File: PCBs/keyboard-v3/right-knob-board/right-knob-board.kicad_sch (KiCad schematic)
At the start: 36 parts, among them J101 F31L-1A7H1-11008, M1 2206-100T, Q101 DMP21D0UFB-7B, Q102 DMP21D0UFB-7B, Q201 DMN21D2UFB-7B, SW1 SW_DIP_x01, SW2 SW_DIP_x01, SW3 SW_DIP_x01, U101 TMC6300-LA, U102 AS5600, U103 STM32U031C6Ux

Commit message: Right control board placement and schematic done
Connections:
- net DIAG: now also U103.25 (PB12); no longer U103.21 (PB10)
- net STANDBY: now also U103.21 (PB10); no longer U103.25 (PB12)
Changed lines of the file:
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@@
 	(wire
 		(pts
-			(xy 35.56 172.72) (xy 48.26 172.72)
-		)
-		(stroke
-			(width 0)
-			(type default)
-		)
-	)
-	(wire
-		(pts
 			(xy 88.9 55.88) (xy 76.2 55.88)
 		)
@@
 	(wire
 		(pts
-			(xy 35.56 177.8) (xy 48.26 177.8)
-		)
-		(stroke
-			(width 0)
-			(type default)
-		)
-	)
-	(wire
-		(pts
 			(xy 139.7 106.68) (xy 139.7 116.84)
 		)
@@
 	(wire
 		(pts
+			(xy 35.56 172.72) (xy 48.26 172.72)
+		)
+		(stroke
+			(width 0)
+			(type default)
+		)
+	)
+	(wire
+		(pts
 			(xy 114.3 96.52) (xy 114.3 99.06)
 		)
@@
 	(wire
 		(pts
+			(xy 35.56 177.8) (xy 48.26 177.8)
+		)
+		(stroke
+			(width 0)
+			(type default)
+		)
+	)
+	(wire
+		(pts
 			(xy 93.98 165.1) (xy 96.52 165.1)
 		)
@@
 		)
 	)
+	(label "DIAG"
+		(at 35.56 177.8 0)
+		(effects
+			(font
+				(size 1.27 1.27)
+			)
+			(justify left bottom)
+		)
+	)
 	(label "STANDBY"
 		(at 167.64 147.32 0)
@@
 		)
 	)
+	(label "STANDBY"
+		(at 35.56 172.72 0)
+		(effects
+			(font
+				(size 1.27 1.27)
+			)
+			(justify left bottom)
+		)
+	)
 	(label "LED2"
 		(at 203.2 45.72 0)
@@
 		)
 	)
-	(label "STANDBY"
-		(at 35.56 177.8 0)
-		(effects
-			(font
-				(size 1.27 1.27)
-			)
-			(justify left bottom)
-		)
-	)
 	(label "DIAG"
 		(at 190.5 134.62 0)
@@
 		)
 	)
-	(label "DIAG"
-		(at 35.56 172.72 0)
-		(effects
-			(font
-				(size 1.27 1.27)
-			)
-			(justify left bottom)
-		)
-	)
 	(label "TX"
 		(at 35.56 170.18 0)
@@
 		)
 		(pin "25"
+			(alternate "TIM1_BKIN")
 		)
 		(pin "38"

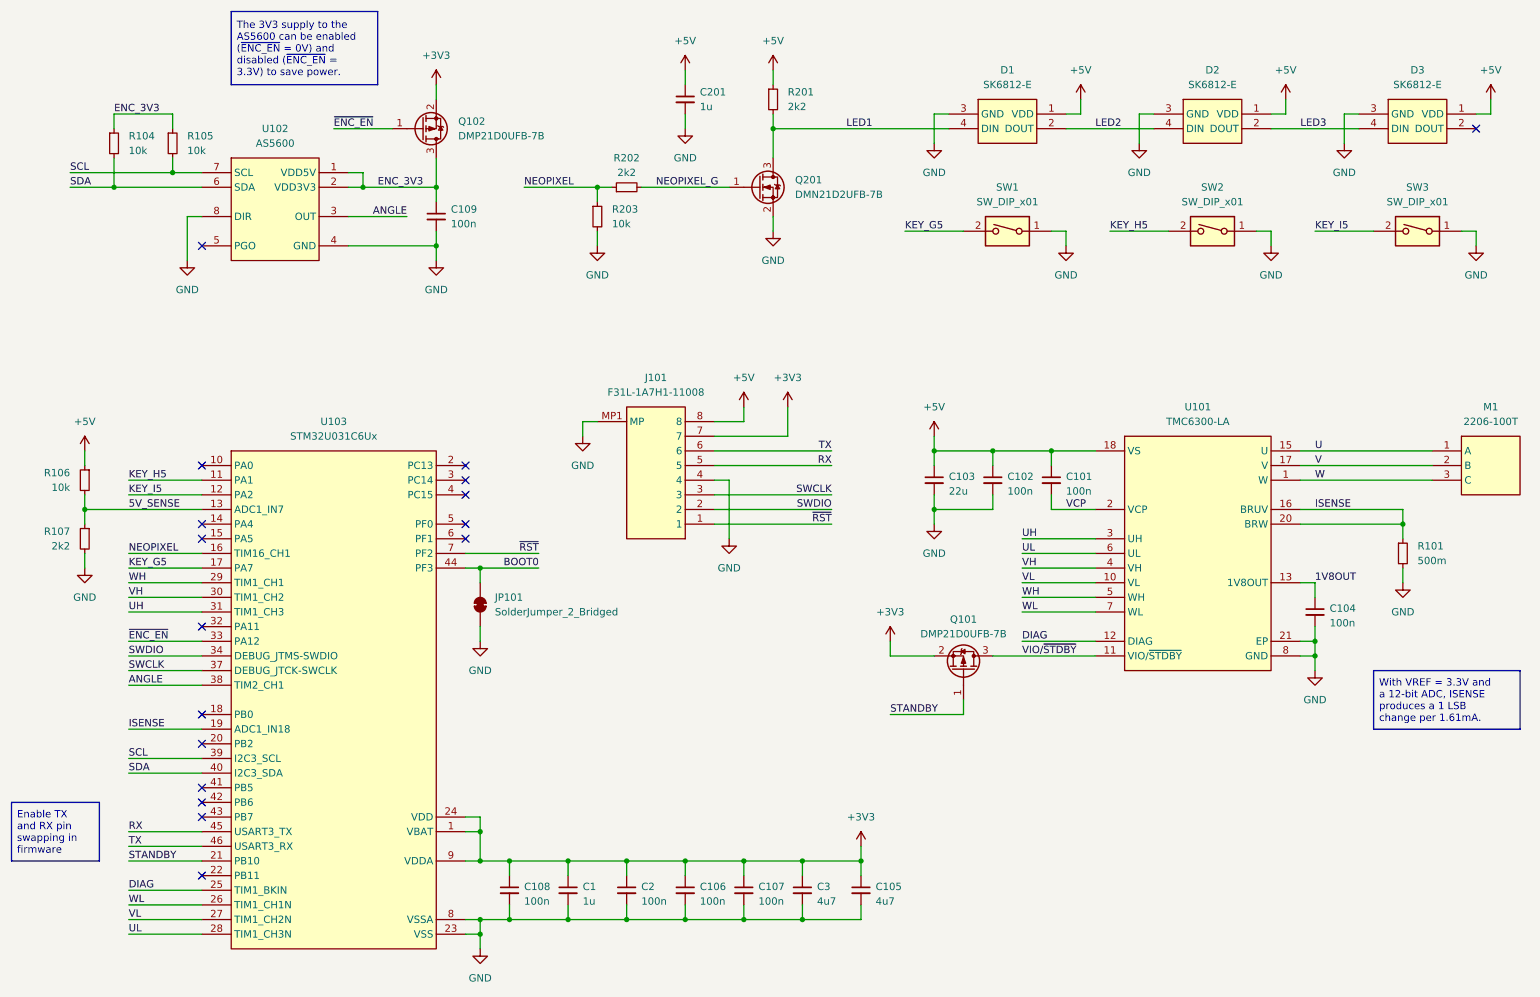
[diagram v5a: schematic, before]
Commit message: Added mounting holes
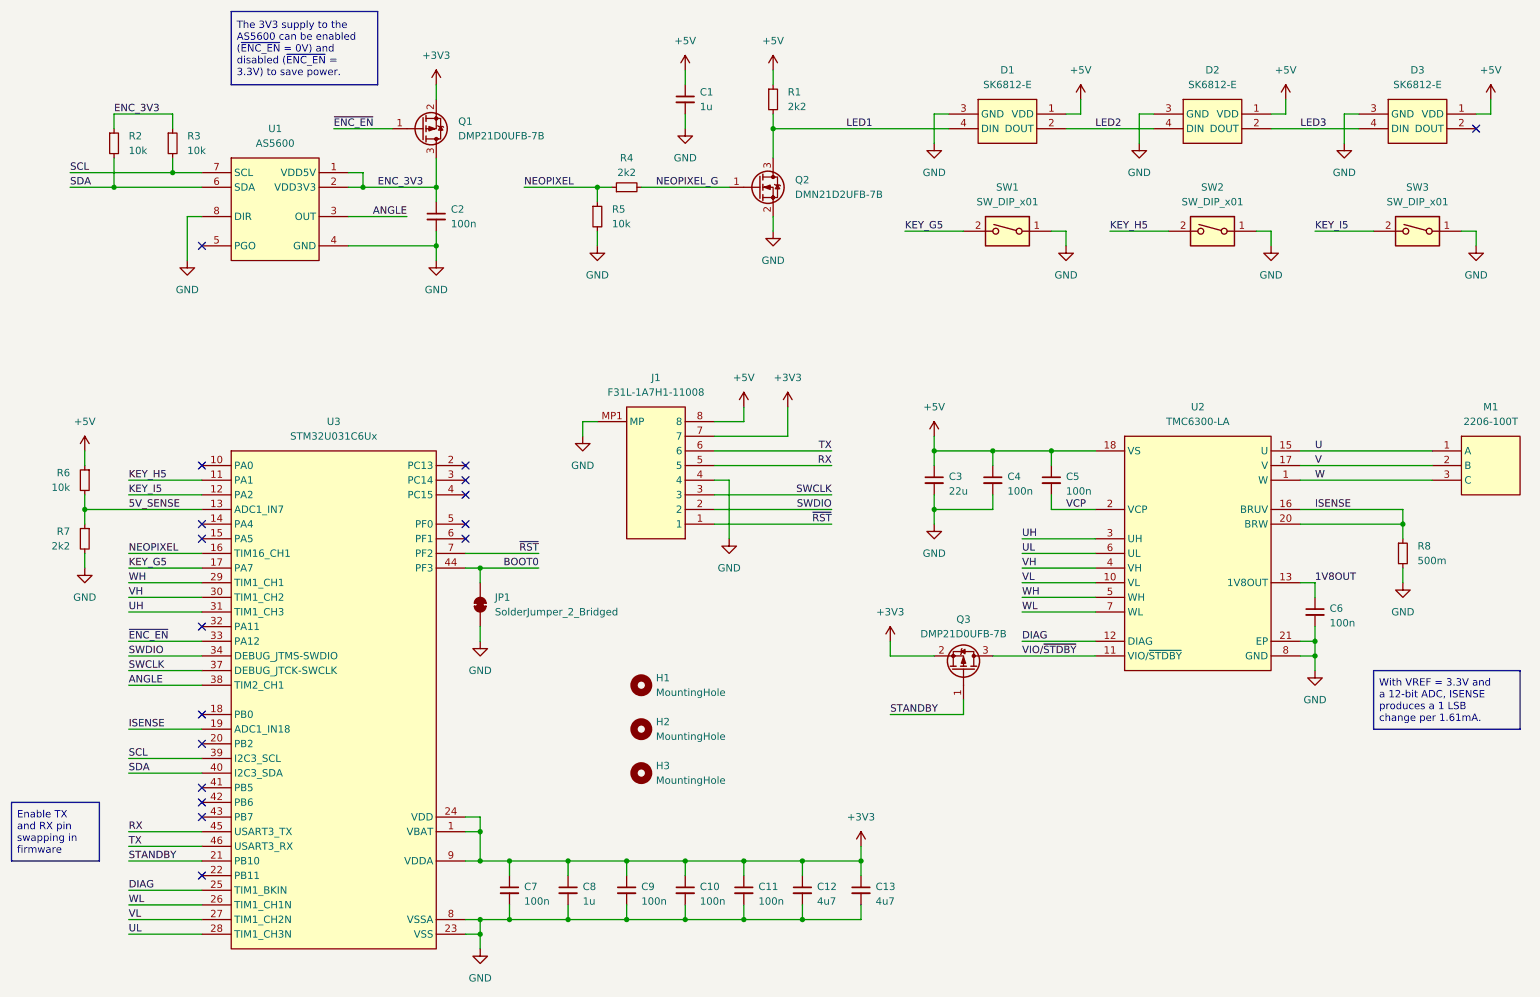
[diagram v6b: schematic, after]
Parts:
- added H1, H2, H3: MountingHole, MountingHole:MountingHole_2.2mm_M2, symbol Mechanical:MountingHole
- renumbered C201 to C1, C106 to C10, C107 to C11, C3 to C12, C105 to C13, C109 to C2, C103 to C3, C102 to C4, C101 to C5, C104 to C6, C108 to C7, C1 to C8, C2 to C9, J101 to J1, JP101 to JP1, Q102 to Q1, Q201 to Q2, Q101 to Q3, R201 to R1, R104 to R2, R105 to R3, R202 to R4, R203 to R5, R106 to R6, R107 to R7, R101 to R8, U102 to U1, U101 to U2, U103 to U3

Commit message: Left key board done
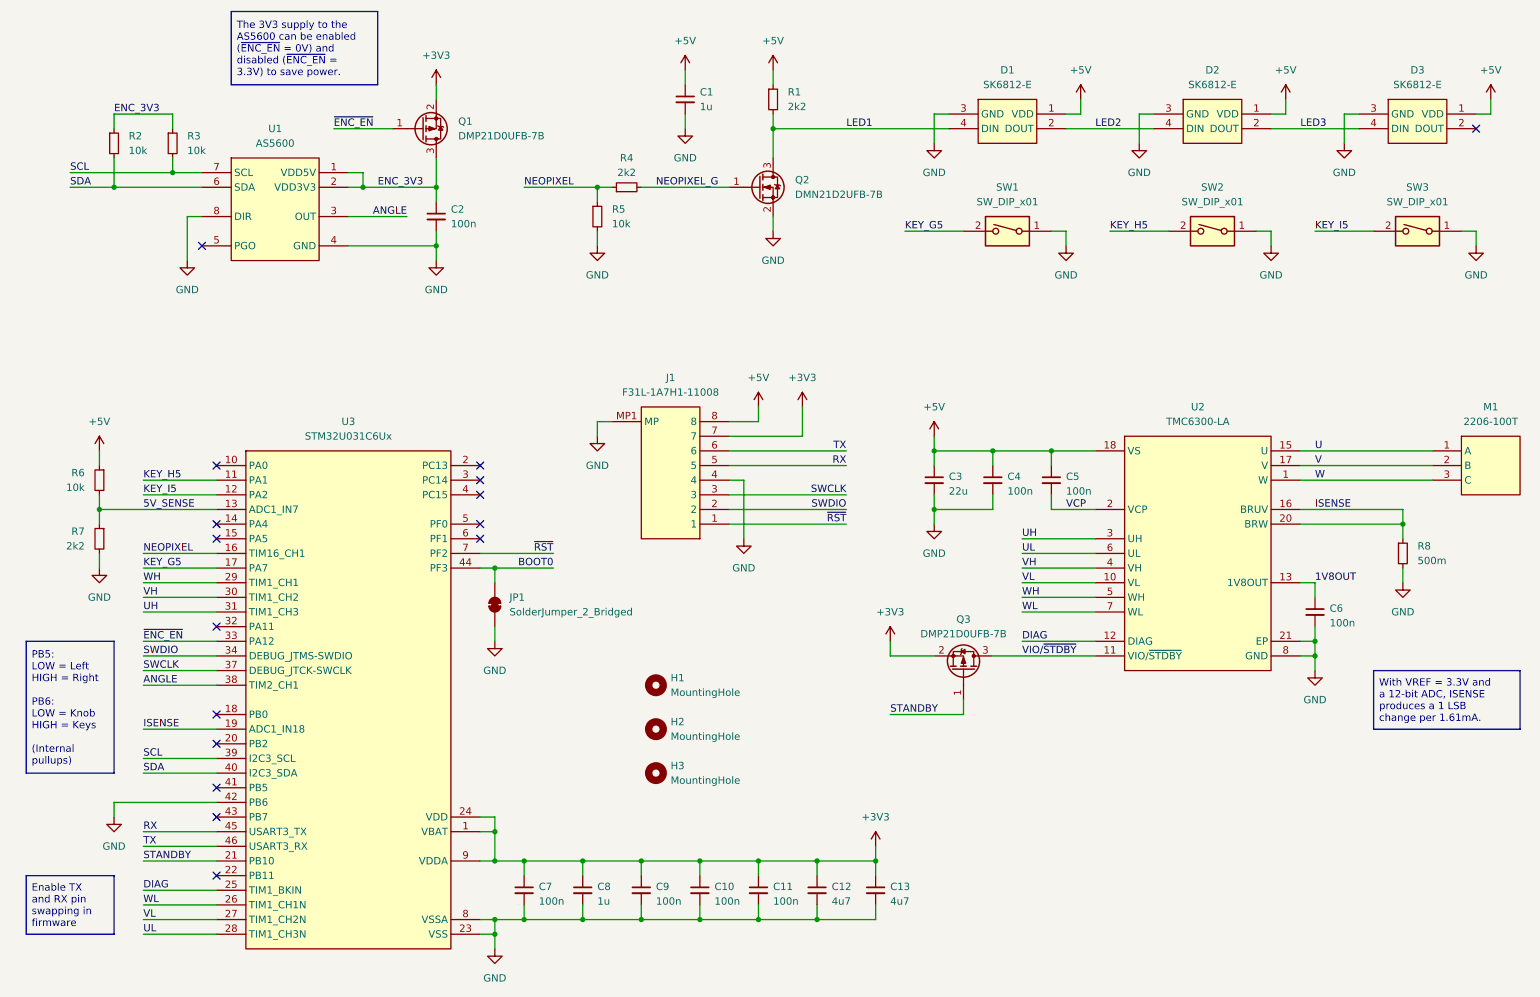
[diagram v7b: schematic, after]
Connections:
- net GND: now also U3.42 (PB6)
- no-connect marks 17 -> 16
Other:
- moved on the sheet: C10, C11, C12, C13, C7, C8, C9, H1, H2, H3, J1, JP1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

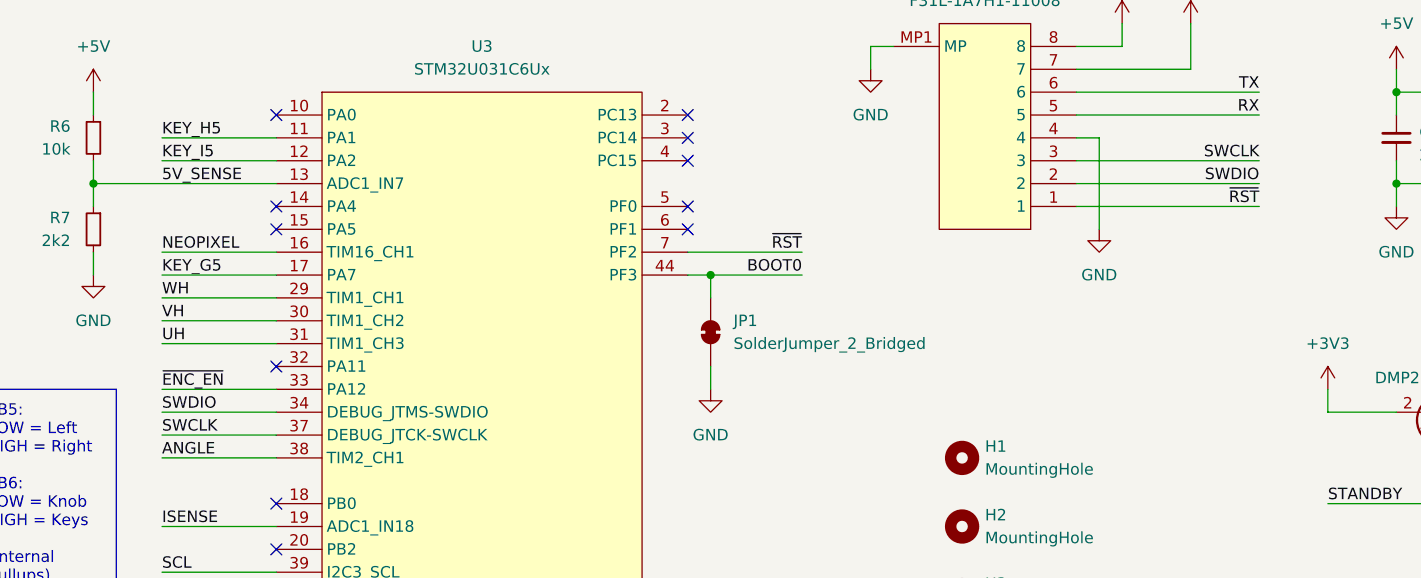
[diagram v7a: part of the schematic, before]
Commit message: Left knob board done
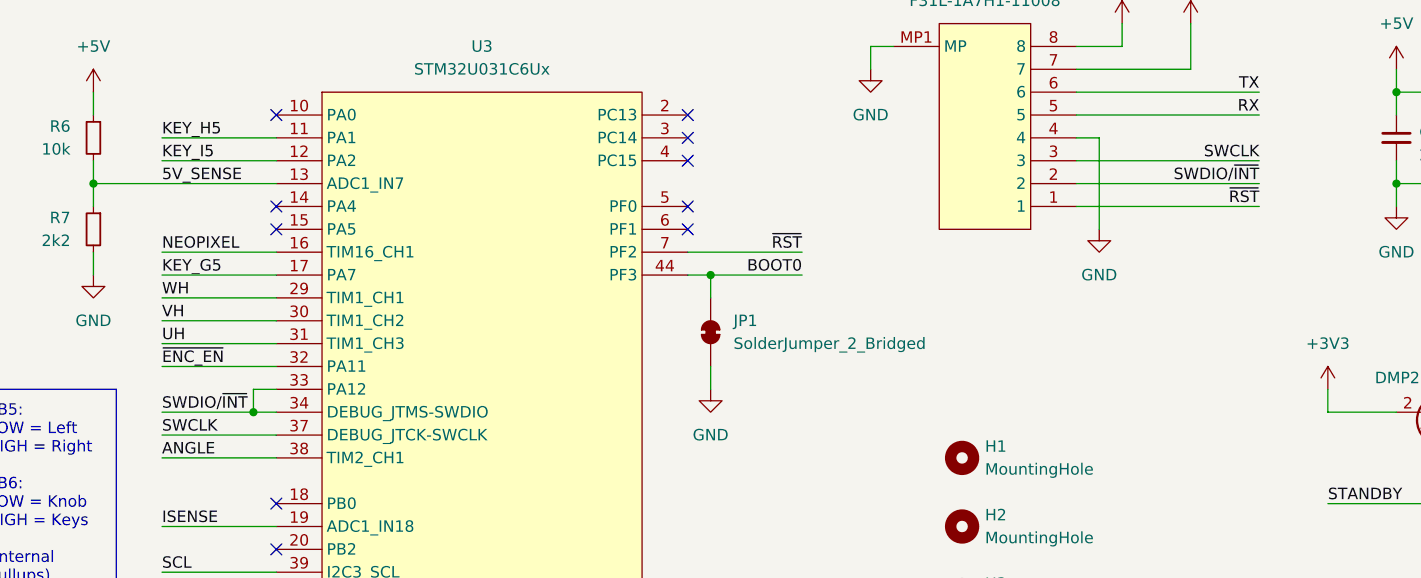
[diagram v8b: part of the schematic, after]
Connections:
- net ~{ENC_EN}: now also U3.32 (PA11); no longer U3.33 (PA12)
- net SWDIO renamed SWDIO/~{INT}
- net SWDIO/~{INT}: now also U3.33 (PA12)
- no-connect marks 16 -> 15
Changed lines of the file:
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@@
+		(color 0 0 0 0)
+	)
+	(junction
+		(at 48.26 137.16)
+		(diameter 0)
 		(color 0 0 0 0)
 	)
@@
 	)
 	(no_connect
-		(at 50.8 132.08)
-	)
-	(no_connect
 		(at 50.8 116.84)
 	)
@@
 	(wire
 		(pts
+			(xy 48.26 137.16) (xy 50.8 137.16)
+		)
+		(stroke
+			(width 0)
+			(type default)
+		)
+	)
+	(wire
+		(pts
 			(xy 139.7 101.6) (xy 160.02 101.6)
 		)
@@
 	(wire
 		(pts
-			(xy 38.1 134.62) (xy 50.8 134.62)
-		)
-		(stroke
-			(width 0)
-			(type default)
-		)
-	)
-	(wire
-		(pts
 			(xy 241.3 137.16) (xy 241.3 134.62)
 		)
@@
 	(wire
 		(pts
+			(xy 48.26 134.62) (xy 48.26 137.16)
+		)
+		(stroke
+			(width 0)
+			(type default)
+		)
+	)
+	(wire
+		(pts
 			(xy 132.08 35.56) (xy 132.08 38.1)
 		)
@@
 	(wire
 		(pts
+			(xy 38.1 132.08) (xy 50.8 132.08)
+		)
+		(stroke
+			(width 0)
+			(type default)
+		)
+	)
+	(wire
+		(pts
 			(xy 180.34 144.78) (xy 180.34 147.32)
 		)
@@
 	(wire
 		(pts
+			(xy 50.8 134.62) (xy 48.26 134.62)
+		)
+		(stroke
+			(width 0)
+			(type default)
+		)
+	)
+	(wire
+		(pts
 			(xy 38.1 139.7) (xy 50.8 139.7)
 		)
@@
 	(wire
 		(pts
-			(xy 38.1 137.16) (xy 50.8 137.16)
+			(xy 38.1 137.16) (xy 48.26 137.16)
 		)
 		(stroke
@@
 		)
 	)
-	(label "~{ENC_EN}"
-		(at 38.1 134.62 0)
-		(effects
-			(font
-				(size 1.27 1.27)
-			)
-			(justify left bottom)
-		)
-	)
 	(label "VCP"
 		(at 198.12 111.76 0)
@@
 		)
 	)
+	(label "SWDIO{slash}~{INT}"
+		(at 160.02 111.76 180)
+		(effects
+			(font
+				(size 1.27 1.27)
+			)
+			(justify right bottom)
+		)
+	)
 	(label "WH"
 		(at 38.1 124.46 0)
@@
 		)
 	)
+	(label "~{ENC_EN}"
+		(at 38.1 132.08 0)
+		(effects
+			(font
+				(size 1.27 1.27)
+			)
+			(justify left bottom)
+		)
+	)
 	(label "U"
 		(at 241.3 101.6 0)
@@
 		)
 	)
-	(label "SWDIO"
+	(label "SWDIO{slash}~{INT}"
 		(at 38.1 137.16 0)
 		(effects
@@
 		)
 	)
-	(label "SWDIO"
-		(at 160.02 111.76 180)
-		(effects
-			(font
-				(size 1.27 1.27)
-			)
-			(justify right bottom)
-		)
-	)
